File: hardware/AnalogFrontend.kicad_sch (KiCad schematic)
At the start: 26 parts, among them J2 Exp1, J3 Exp2, J4 Exp3, J5 Exp4, U4 AD7718, U5 AD7718, Y1 MS1V-T1K-32.768kHz-12.5pF-20P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, Y2 MS1V-T1K-32.768kHz-12.5pF-20P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

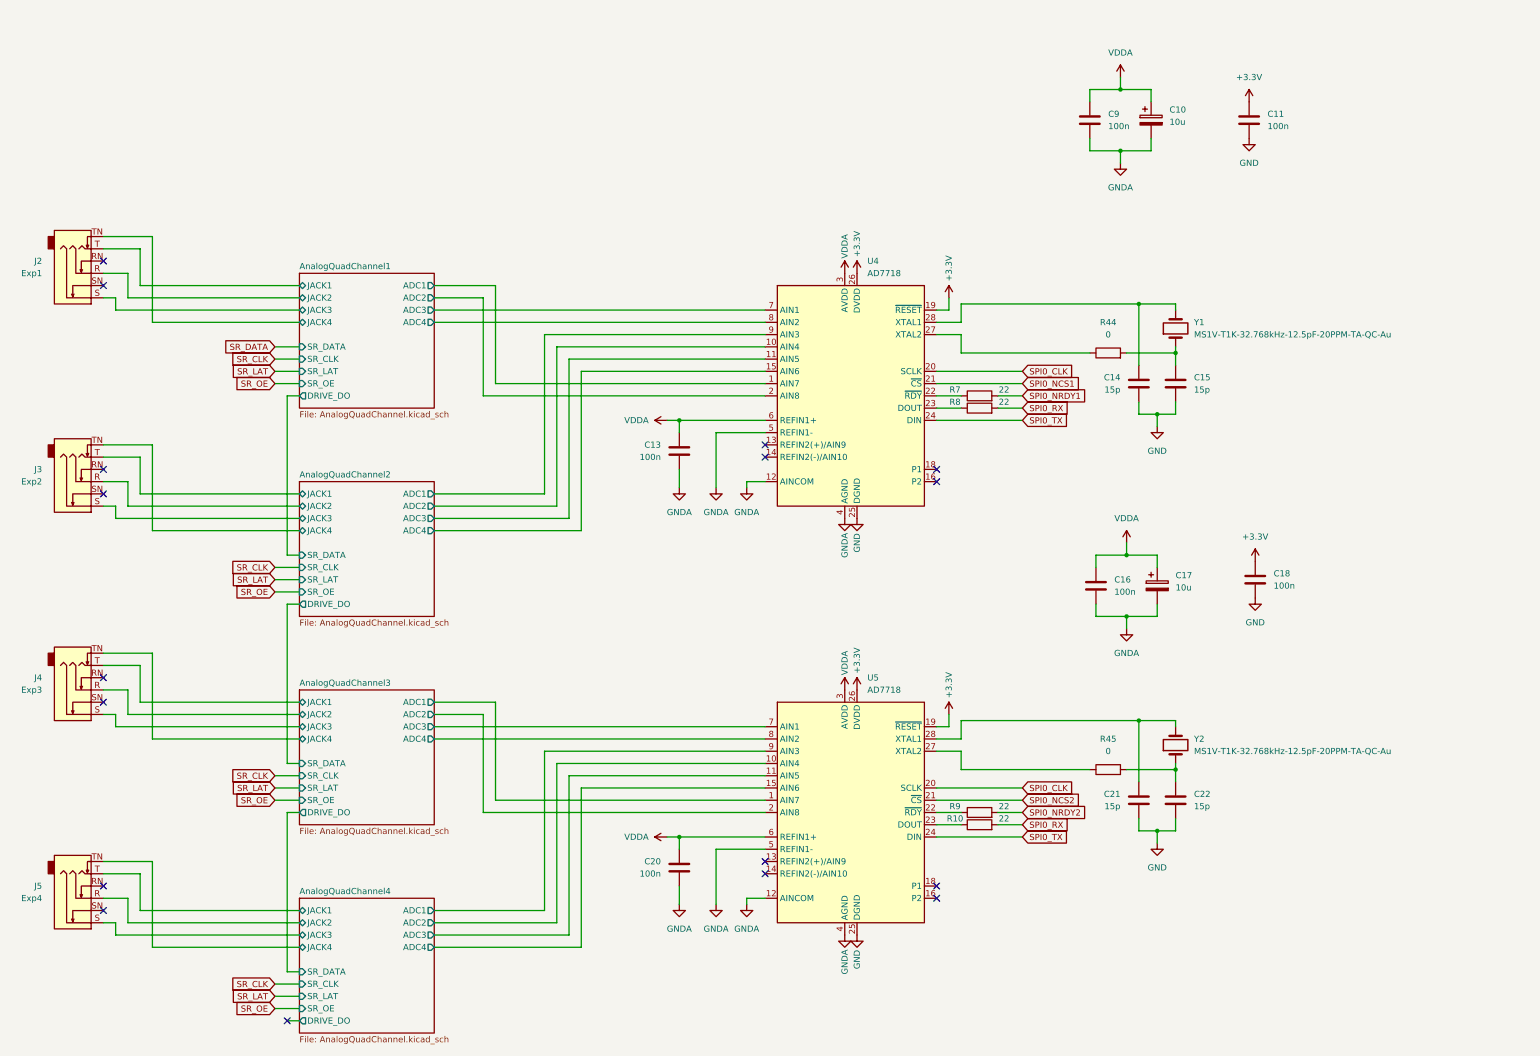
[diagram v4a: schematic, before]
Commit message: very tight layout
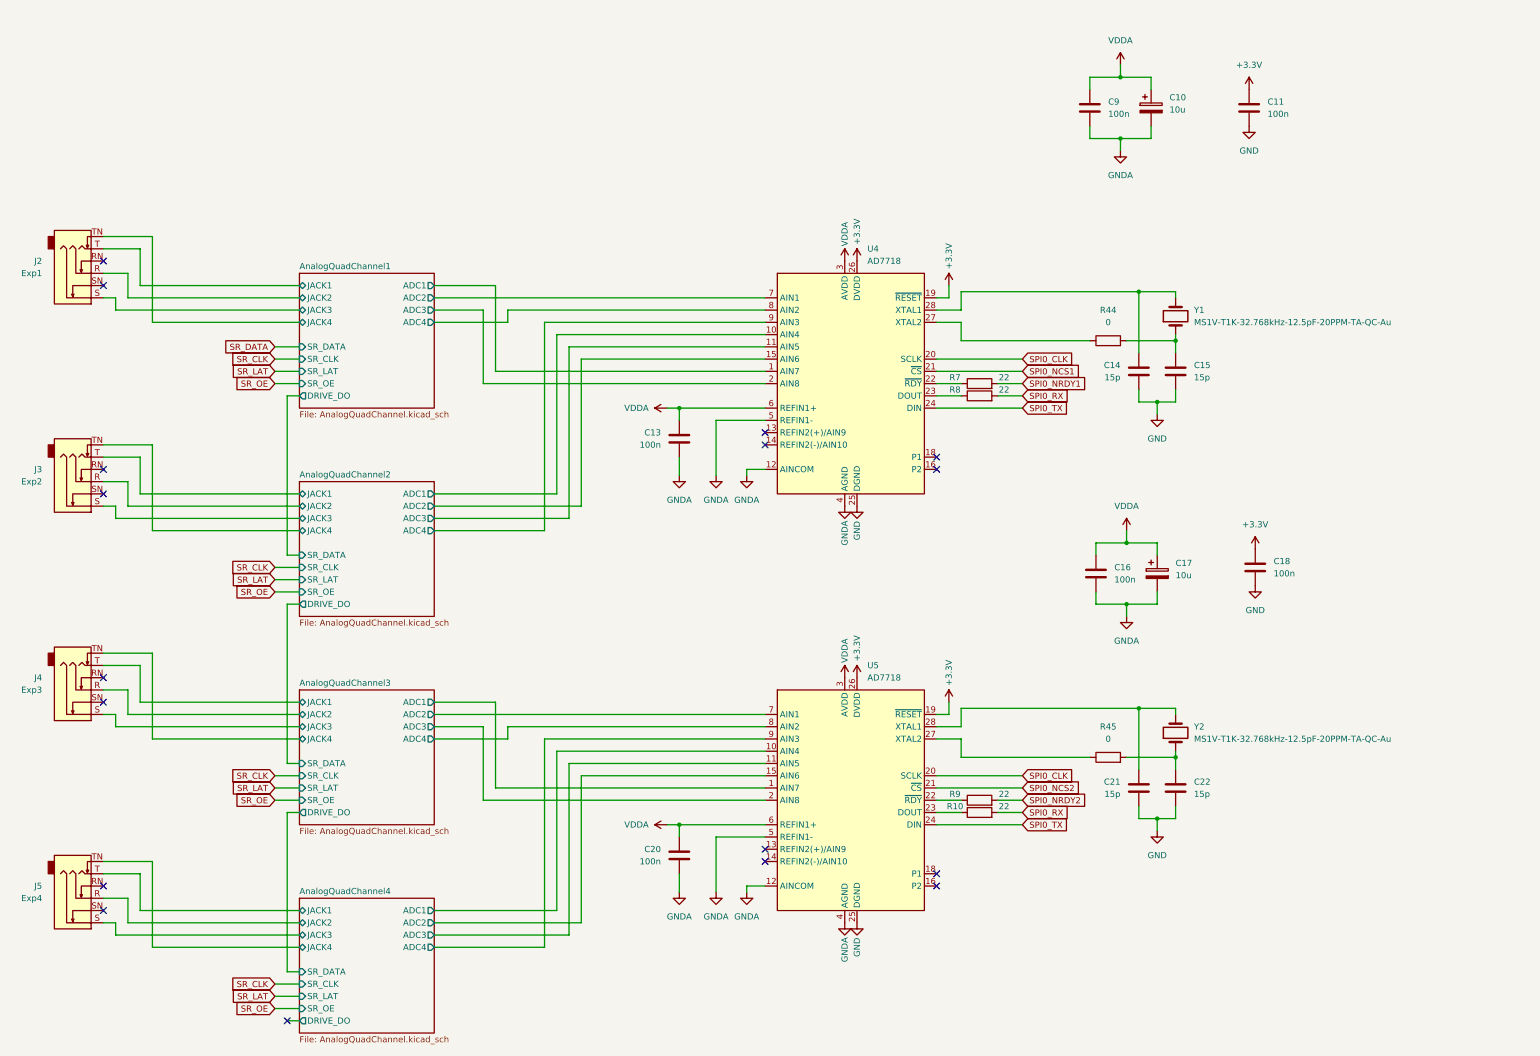
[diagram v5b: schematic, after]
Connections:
- net AnalogQuadChannel1/ADC2: now also U4.7 (AIN1); no longer U4.2 (AIN8)
- net AnalogQuadChannel1/ADC3: now also U4.2 (AIN8); no longer U4.7 (AIN1)
- net AnalogQuadChannel2/ADC1: now also U4.10 (AIN4); no longer U4.9 (AIN3)
- net AnalogQuadChannel2/ADC2: now also U4.15 (AIN6); no longer U4.10 (AIN4)
- net AnalogQuadChannel2/ADC4: now also U4.9 (AIN3); no longer U4.15 (AIN6)
- net AnalogQuadChannel3/ADC2: now also U5.7 (AIN1); no longer U5.2 (AIN8)
- net AnalogQuadChannel3/ADC3: now also U5.2 (AIN8); no longer U5.7 (AIN1)
- net AnalogQuadChannel4/ADC1: now also U5.10 (AIN4); no longer U5.9 (AIN3)
- net AnalogQuadChannel4/ADC2: now also U5.15 (AIN6); no longer U5.10 (AIN4)
- net AnalogQuadChannel4/ADC4: now also U5.9 (AIN3); no longer U5.15 (AIN6)
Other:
- moved on the sheet: C10, C11, C13, C14, C15, C16, C17, C18, C20, C21, C22, C9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

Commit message: schematic updates
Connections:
- net VDDA: no longer C13.1, C20.1, U4.6 (REFIN1+), U5.6 (REFIN1+)
- new net +2.5V: C13.1, C20.1, U4.6 (REFIN1+), U5.6 (REFIN1+)
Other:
- moved on the sheet: C13, C20

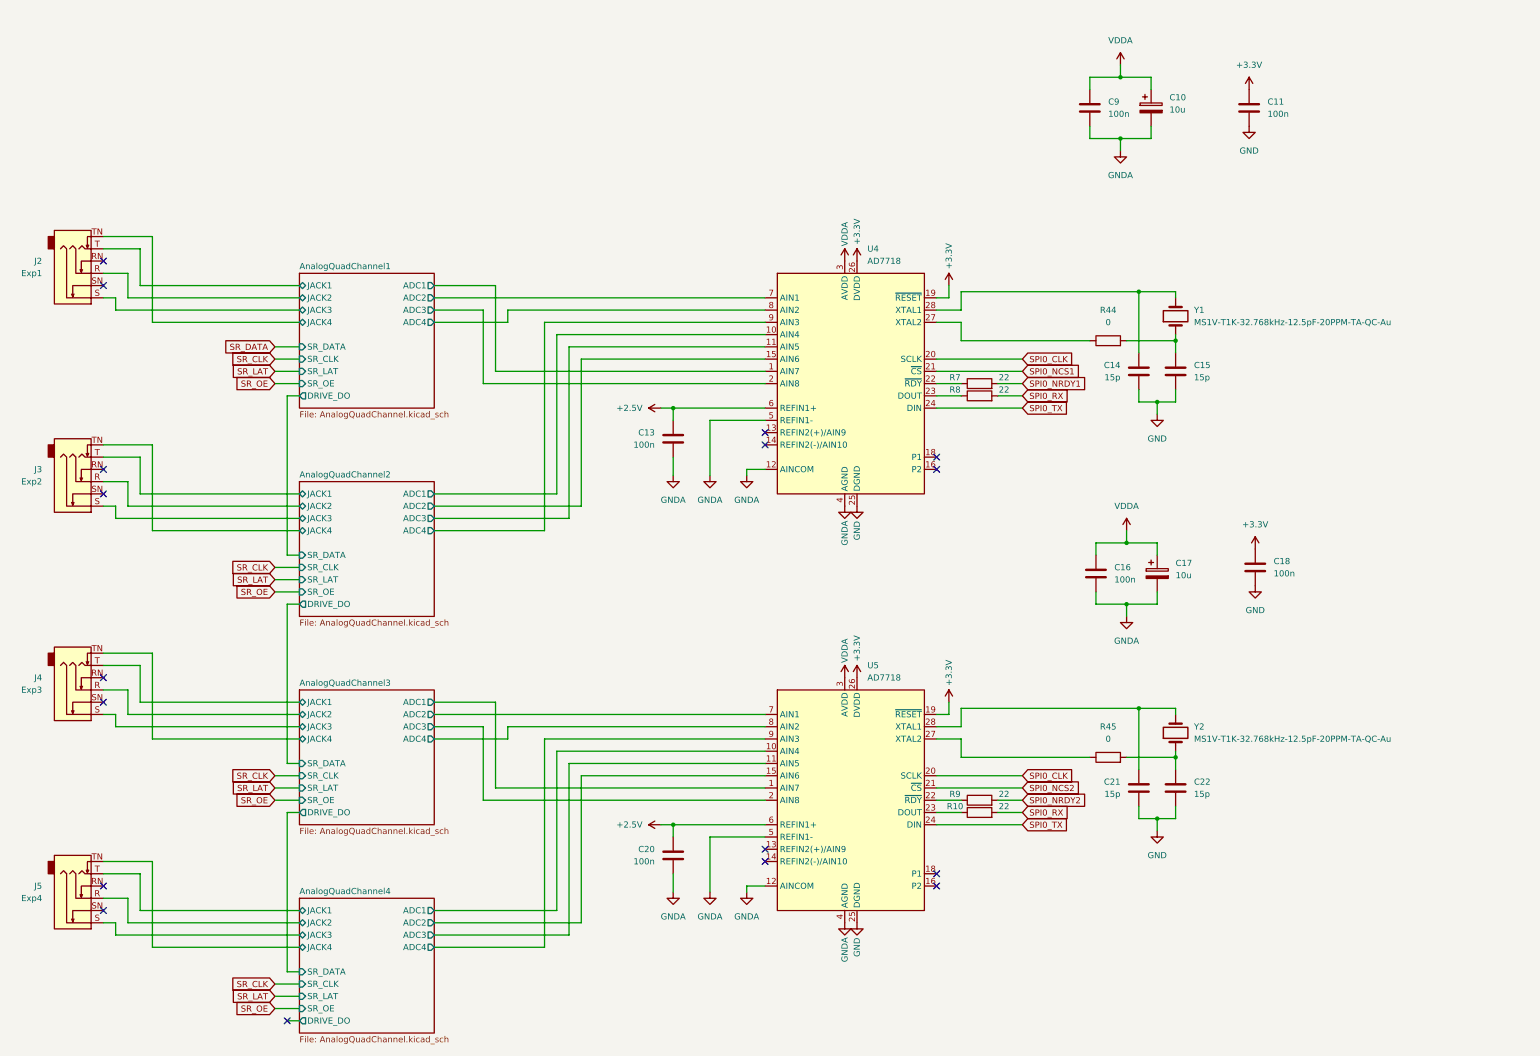
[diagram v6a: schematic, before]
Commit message: replaced buffer ICs with analog switches, schematic bugfixes, started new routing
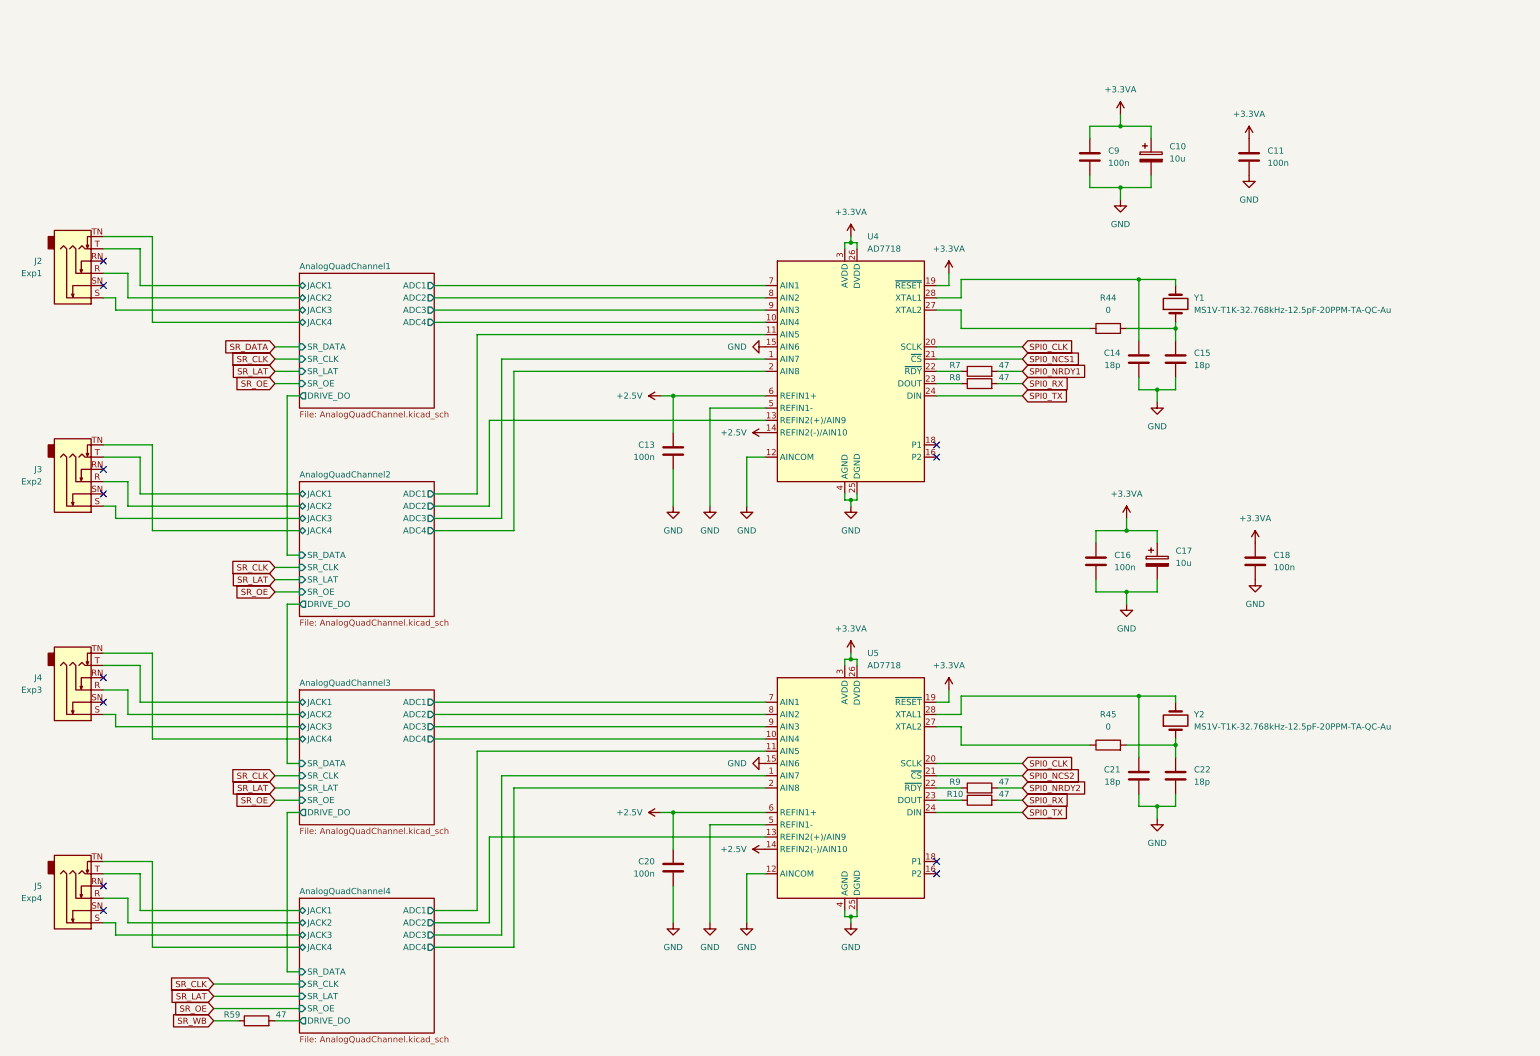
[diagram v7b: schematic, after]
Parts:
- added R59: 47, Resistor_SMD:R_0805_2012Metric, symbol Device:R
- C14, C15, C21, C22: value 15p -> 18p
- R10, R7, R8, R9: value 22 -> 47
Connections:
- net GND is gone; now on net AGND: C11.2, C14.2, C15.2, C18.2, C21.2, C22.2, U4.25 (DGND), U5.25 (DGND)
- net VDDA is gone; now on net +3.3VA: C10.1, C16.1, C17.1, C9.1, U4.3 (AVDD), U5.3 (AVDD)
- net +2.5V: now also U4.14 (REFIN2(-)/AIN10), U5.14 (REFIN2(-)/AIN10)
- net AGND: now also U4.15 (AIN6), U5.15 (AIN6)
- net AnalogQuadChannel1/ADC1: now also U4.7 (AIN1); no longer U4.1 (AIN7)
- net AnalogQuadChannel1/ADC2: now also U4.8 (AIN2); no longer U4.7 (AIN1)
- net AnalogQuadChannel1/ADC3: now also U4.9 (AIN3); no longer U4.2 (AIN8)
- net AnalogQuadChannel1/ADC4: now also U4.10 (AIN4); no longer U4.8 (AIN2)
- net AnalogQuadChannel2/ADC1: now also U4.11 (AIN5); no longer U4.10 (AIN4)
- net AnalogQuadChannel2/ADC2: now also U4.13 (REFIN2(+)/AIN9); no longer U4.15 (AIN6)
- net AnalogQuadChannel2/ADC3: now also U4.1 (AIN7); no longer U4.11 (AIN5)
- net AnalogQuadChannel2/ADC4: now also U4.2 (AIN8); no longer U4.9 (AIN3)
- net AnalogQuadChannel3/ADC1: now also U5.7 (AIN1); no longer U5.1 (AIN7)
- net AnalogQuadChannel3/ADC2: now also U5.8 (AIN2); no longer U5.7 (AIN1)
- net AnalogQuadChannel3/ADC3: now also U5.9 (AIN3); no longer U5.2 (AIN8)
- net AnalogQuadChannel3/ADC4: now also U5.10 (AIN4); no longer U5.8 (AIN2)
- net AnalogQuadChannel4/ADC1: now also U5.11 (AIN5); no longer U5.10 (AIN4)
- net AnalogQuadChannel4/ADC2: now also U5.13 (REFIN2(+)/AIN9); no longer U5.15 (AIN6)
- net AnalogQuadChannel4/ADC3: now also U5.1 (AIN7); no longer U5.11 (AIN5)
- net AnalogQuadChannel4/ADC4: now also U5.2 (AIN8); no longer U5.9 (AIN3)
- net AnalogQuadChannel4/DRIVE_DO: now also R59.2
- net +3.3V renamed +3.3VA
- new net SR_WB: R59.1
- no-connect marks 17 -> 12
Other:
- moved on the sheet: C10, C11, C13, C14, C15, C16, C17, C18, C20, C21, C22, C9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

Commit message: new PCB updates
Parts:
- C10: footprint Capacitor_SMD:C_1210_3225Metric -> Capacitor_SMD:C_0805_2012Metric
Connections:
- net AnalogQuadChannel1/ADC1: now also U4.2 (AIN8); no longer U4.7 (AIN1)
- net AnalogQuadChannel1/ADC2: now also U4.7 (AIN1); no longer U4.8 (AIN2)
- net AnalogQuadChannel1/ADC3: now also U4.1 (AIN7); no longer U4.9 (AIN3)
- net AnalogQuadChannel1/ADC4: now also U4.8 (AIN2); no longer U4.10 (AIN4)
- net AnalogQuadChannel2/ADC1: now also U4.9 (AIN3); no longer U4.11 (AIN5)
- net AnalogQuadChannel2/ADC3: now also U4.10 (AIN4); no longer U4.1 (AIN7)
- net AnalogQuadChannel2/ADC4: now also U4.11 (AIN5); no longer U4.2 (AIN8)
- net AnalogQuadChannel3/ADC1: now also U5.2 (AIN8); no longer U5.7 (AIN1)
- net AnalogQuadChannel3/ADC2: now also U5.7 (AIN1); no longer U5.8 (AIN2)
- net AnalogQuadChannel3/ADC3: now also U5.1 (AIN7); no longer U5.9 (AIN3)
- net AnalogQuadChannel3/ADC4: now also U5.8 (AIN2); no longer U5.10 (AIN4)
- net AnalogQuadChannel4/ADC1: now also U5.9 (AIN3); no longer U5.11 (AIN5)
- net AnalogQuadChannel4/ADC3: now also U5.10 (AIN4); no longer U5.1 (AIN7)
- net AnalogQuadChannel4/ADC4: now also U5.11 (AIN5); no longer U5.2 (AIN8)
